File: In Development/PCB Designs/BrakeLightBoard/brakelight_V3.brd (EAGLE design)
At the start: 68.6 x 38.1 mm, 21 parts, among them Q2 30N06L

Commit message: Created brakelight board v3 board
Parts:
- moved R8 108.1 mm to (65.4, 16.6), turned to 270 degrees
- moved D2 99.1 mm to (65.4, 25.3), turned to 270 degrees
- moved R6 94.3 mm to (59.9, 32.3), turned to 270 degrees
- moved D4 93.2 mm to (58.4, 13.8)
- moved R7 84.0 mm to (39.1, 11.3), turned to 90 degrees
- moved D3 80.2 mm to (46.4, 13.9), turned to 180 degrees
- moved R4 77.8 mm to (57.6, 22.4), turned to 180 degrees
- moved R5 66.1 mm to (38.2, 19.6), turned to 90 degrees
- moved D1 61.1 mm to (32.6, 8.66)
- moved R2 49.9 mm to (36.9, 25.5), turned to 180 degrees
- moved R3 46.0 mm to (30.7, 18.4), turned to 180 degrees
- moved R1 41.8 mm to (29.7, 25.5)
- moved U$1 15.0 mm to (19.6, 23.1)
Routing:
- net GND: track 71.5 -> 0.00 mm
- net VCC: track 146.1 -> 89.0 mm
- net 5V: track 108.6 -> 62.7 mm
- net N$1: track 0.00 -> 30.3 mm
- net N$7: track 0.00 -> 15.3 mm
- net N$2: track 86.3 -> 74.4 mm
- net THRESH1: track 9.70 -> 21.1 mm
- net THRESH2: track 7.25 -> 15.8 mm
- net PT2: track 21.3 -> 29.1 mm
- net PT1: track 51.2 -> 46.1 mm
- net N$3: track 0.00 -> 3.50 mm
- net N$4: track 0.00 -> 3.21 mm
- net N$5: track 0.00 -> 2.71 mm
- net N$6: track 0.00 -> 2.39 mm

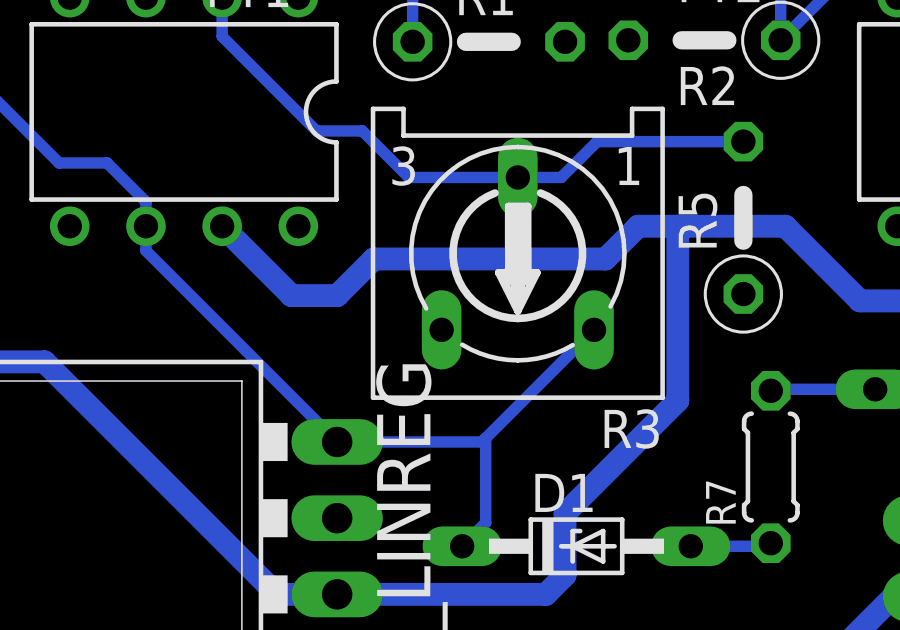
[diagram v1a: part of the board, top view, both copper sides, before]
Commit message: Improved brakelight v3 ground plane connections
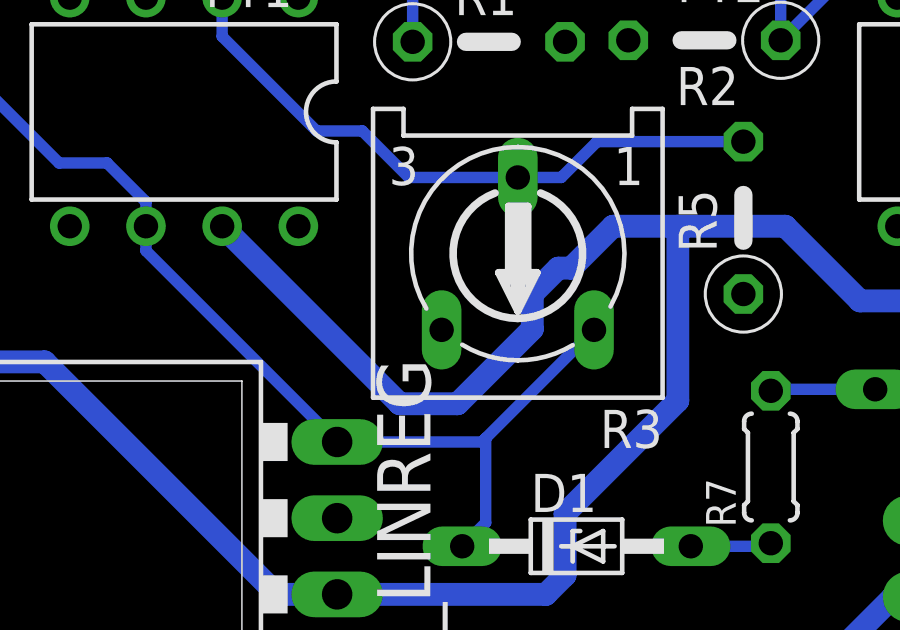
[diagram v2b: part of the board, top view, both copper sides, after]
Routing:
- net VCC: track 89.0 -> 92.7 mm
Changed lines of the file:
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@@
 <vertex x="0" y="0"/>
 </polygon>
-<wire x1="43.3324" y1="26.9494" x2="42.9332" y2="32.4626" width="0" layer="19" extent="1-1"/>
-<wire x1="15.748" y1="26.9494" x2="15.748" y2="19.3294" width="0" layer="19" extent="1-1"/>
 </signal>
 <signal name="N$2">
@@
 <wire x1="4.0894" y1="21.1858" x2="6.9464" y2="18.3288" width="0.762" layer="16"/>
 <wire x1="4.0894" y1="26.2578" x2="4.0894" y2="21.1858" width="0.762" layer="16"/>
-<wire x1="20.828" y1="19.3294" x2="23.1394" y2="17.018" width="0.762" layer="16"/>
-<wire x1="23.1394" y1="17.018" x2="24.6634" y2="17.018" width="0.762" layer="16"/>
-<wire x1="33.6042" y1="18.2372" x2="34.6964" y2="19.3294" width="0.762" layer="16"/>
-<wire x1="34.6964" y1="19.3294" x2="36.0172" y2="19.3294" width="0.762" layer="16"/>
 <wire x1="36.0172" y1="19.3294" x2="39.5986" y2="19.3294" width="0.762" layer="16"/>
 <wire x1="42.0878" y1="16.8402" x2="47.2694" y2="16.8402" width="0.762" layer="16"/>
 <wire x1="47.2694" y1="16.8402" x2="48.4124" y2="17.9832" width="0.762" layer="16"/>
 <wire x1="48.4124" y1="17.9832" x2="48.4124" y2="19.3294" width="0.762" layer="16"/>
-<wire x1="24.6634" y1="17.018" x2="25.8826" y2="18.2372" width="0.762" layer="16"/>
-<wire x1="25.8826" y1="18.2372" x2="33.6042" y2="18.2372" width="0.762" layer="16"/>
 <wire x1="39.5986" y1="19.3294" x2="42.0878" y2="16.8402" width="0.762" layer="16"/>
 <wire x1="36.0172" y1="19.3294" x2="36.0172" y2="13.5128" width="0.762" layer="16"/>
@@
 <wire x1="31.6194" y1="7.0576" x2="24.6612" y2="7.0576" width="0.762" layer="16"/>
 <wire x1="36.0172" y1="13.5128" x2="32.258" y2="9.7536" width="0.762" layer="16"/>
+<wire x1="32.4612" y1="17.9324" x2="32.0294" y2="17.9324" width="0.762" layer="16"/>
+<wire x1="32.0294" y1="17.9324" x2="31.1658" y2="17.0688" width="0.762" layer="16"/>
+<wire x1="26.7462" y1="13.4112" x2="20.828" y2="19.3294" width="0.762" layer="16"/>
+<wire x1="36.0172" y1="19.3294" x2="33.8582" y2="19.3294" width="0.762" layer="16"/>
+<wire x1="33.8582" y1="19.3294" x2="32.4612" y2="17.9324" width="0.762" layer="16"/>
+<wire x1="31.1658" y1="17.0688" x2="31.1658" y2="15.9004" width="0.762" layer="16"/>
+<wire x1="31.1658" y1="15.9004" x2="28.6766" y2="13.4112" width="0.762" layer="16"/>
+<wire x1="28.6766" y1="13.4112" x2="26.7462" y2="13.4112" width="0.762" layer="16"/>
 </signal>
 <signal name="N$1">

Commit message: Added missing resistor values
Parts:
- R7, R8: value (none) -> 1k
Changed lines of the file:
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@@
 <attribute name="VALUE" x="56.134" y="11.176" size="1.27" layer="27" ratio="10"/>
 </element>
-<element name="R7" library="0ohmresistor" package="0204/5" package3d_urn="urn:adsk.eagle:package:23488/1" value="" x="39.116" y="11.303" smashed="yes" rot="R90">
+<element name="R7" library="0ohmresistor" package="0204/5" package3d_urn="urn:adsk.eagle:package:23488/1" value="1k" x="39.116" y="11.303" smashed="yes" rot="R90">
 <attribute name="NAME" x="37.9476" y="9.2964" size="0.9906" layer="25" ratio="10" rot="R90"/>
 <attribute name="POPULARITY" value="18" x="39.116" y="11.303" size="1.778" layer="27" rot="R90" display="off"/>
@@
 <attribute name="VALUE" x="41.4274" y="9.1694" size="0.9906" layer="27" ratio="10" rot="R90"/>
 </element>
-<element name="R8" library="0ohmresistor" package="0204/5" package3d_urn="urn:adsk.eagle:package:23488/1" value="" x="65.3542" y="16.5862" smashed="yes" rot="R270">
+<element name="R8" library="0ohmresistor" package="0204/5" package3d_urn="urn:adsk.eagle:package:23488/1" value="1k" x="65.3542" y="16.5862" smashed="yes" rot="R270">
 <attribute name="NAME" x="66.5226" y="18.5928" size="0.9906" layer="25" ratio="10" rot="R270"/>
 <attribute name="POPULARITY" value="18" x="65.3542" y="16.5862" size="1.778" layer="27" rot="R270" display="off"/>

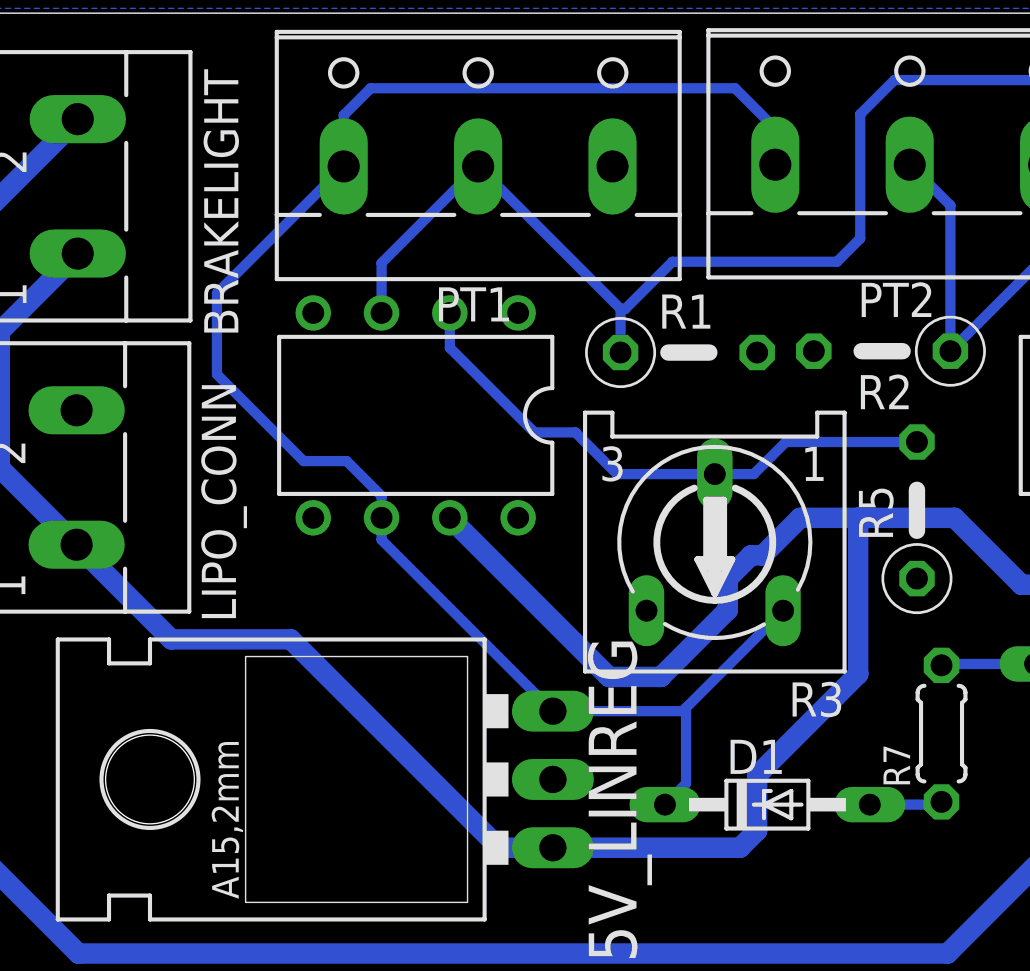
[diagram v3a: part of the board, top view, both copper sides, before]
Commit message: Created new brakelight board using TLC2252
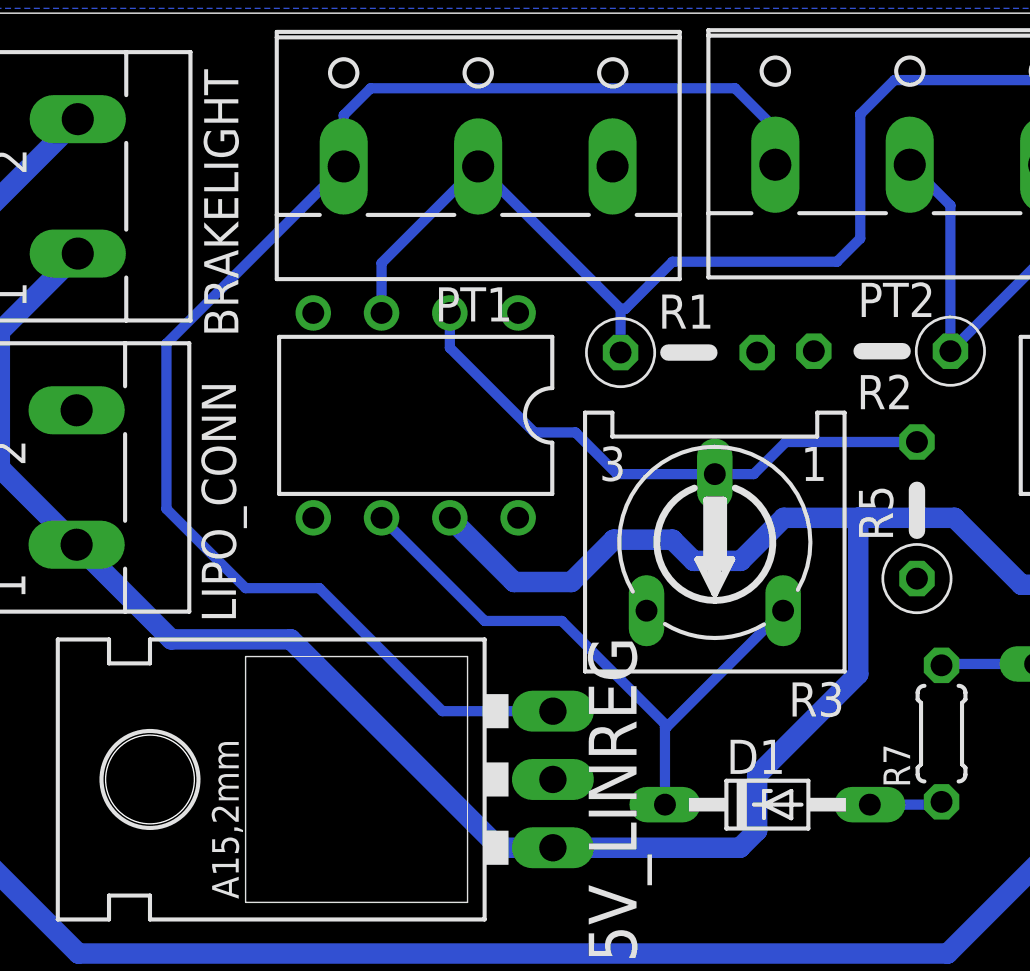
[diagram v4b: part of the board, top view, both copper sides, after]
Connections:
- new net N$8: D1.C, R3.A, U$1.6
- net 5V: no longer D1.C, R3.A, U$1.6
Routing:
- net N$8: track 0.00 -> 22.9 mm
- net 5V: track 62.7 -> 53.3 mm
- net VCC: track 92.7 -> 89.7 mm
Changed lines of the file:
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@@
 <contactref element="PT1" pad="1"/>
 <contactref element="PT2" pad="1"/>
-<contactref element="U$1" pad="6"/>
-<contactref element="R3" pad="A"/>
-<contactref element="D1" pad="C"/>
-<wire x1="33.2232" y1="15.875" x2="29.6128" y2="12.2646" width="0.381" layer="16"/>
-<wire x1="29.6128" y1="12.2646" x2="29.4858" y2="12.1376" width="0.381" layer="16"/>
-<wire x1="29.4858" y1="12.1376" x2="24.6612" y2="12.1376" width="0.381" layer="16"/>
-<wire x1="28.829" y1="8.6614" x2="29.6128" y2="9.4452" width="0.381" layer="16"/>
-<wire x1="29.6128" y1="9.4452" x2="29.6128" y2="12.2646" width="0.381" layer="16"/>
 <wire x1="17.8826" y1="35.306" x2="16.8802" y2="34.3036" width="0.381" layer="16"/>
 <wire x1="16.8802" y1="32.3986" x2="16.8802" y2="34.3036" width="0.381" layer="16"/>
@@
 <wire x1="32.9332" y1="33.8088" x2="32.9332" y2="32.4626" width="0.381" layer="16"/>
 <wire x1="17.8826" y1="35.306" x2="31.436" y2="35.306" width="0.381" layer="16"/>
-<wire x1="18.288" y1="19.3294" x2="18.288" y2="18.5108" width="0.381" layer="16"/>
-<wire x1="18.288" y1="18.5108" x2="24.6612" y2="12.1376" width="0.381" layer="16"/>
-<wire x1="16.8802" y1="32.3986" x2="12.1666" y2="27.685" width="0.381" layer="16"/>
-<wire x1="12.1666" y1="27.685" x2="12.1666" y2="24.6634" width="0.381" layer="16"/>
-<wire x1="12.1666" y1="24.6634" x2="15.3924" y2="21.4376" width="0.381" layer="16"/>
-<wire x1="15.3924" y1="21.4376" x2="16.9926" y2="21.4376" width="0.381" layer="16"/>
-<wire x1="16.9926" y1="21.4376" x2="18.288" y2="20.1422" width="0.381" layer="16"/>
-<wire x1="18.288" y1="20.1422" x2="18.288" y2="19.3294" width="0.381" layer="16"/>
+<wire x1="16.8802" y1="32.3986" x2="10.287" y2="25.8054" width="0.381" layer="16"/>
+<wire x1="10.287" y1="25.8054" x2="10.287" y2="19.6596" width="0.381" layer="16"/>
+<wire x1="20.5522" y1="12.1376" x2="24.6612" y2="12.1376" width="0.381" layer="16"/>
+<wire x1="10.287" y1="19.6596" x2="13.2334" y2="16.7132" width="0.381" layer="16"/>
+<wire x1="13.2334" y1="16.7132" x2="15.9766" y2="16.7132" width="0.381" layer="16"/>
+<wire x1="15.9766" y1="16.7132" x2="20.5522" y2="12.1376" width="0.381" layer="16"/>
 </signal>
 <signal name="PT2">
@@
 <wire x1="31.6194" y1="7.0576" x2="24.6612" y2="7.0576" width="0.762" layer="16"/>
 <wire x1="36.0172" y1="13.5128" x2="32.258" y2="9.7536" width="0.762" layer="16"/>
-<wire x1="32.4612" y1="17.9324" x2="32.0294" y2="17.9324" width="0.762" layer="16"/>
-<wire x1="32.0294" y1="17.9324" x2="31.1658" y2="17.0688" width="0.762" layer="16"/>
-<wire x1="26.7462" y1="13.4112" x2="20.828" y2="19.3294" width="0.762" layer="16"/>
-<wire x1="36.0172" y1="19.3294" x2="33.8582" y2="19.3294" width="0.762" layer="16"/>
-<wire x1="33.8582" y1="19.3294" x2="32.4612" y2="17.9324" width="0.762" layer="16"/>
-<wire x1="31.1658" y1="17.0688" x2="31.1658" y2="15.9004" width="0.762" layer="16"/>
-<wire x1="31.1658" y1="15.9004" x2="28.6766" y2="13.4112" width="0.762" layer="16"/>
-<wire x1="28.6766" y1="13.4112" x2="26.7462" y2="13.4112" width="0.762" layer="16"/>
+<wire x1="33.2486" y1="19.3294" x2="36.0172" y2="19.3294" width="0.762" layer="16"/>
+<wire x1="23.2156" y1="16.9418" x2="25.3492" y2="16.9418" width="0.762" layer="16"/>
+<wire x1="25.3492" y1="16.9418" x2="26.924" y2="18.5166" width="0.762" layer="16"/>
+<wire x1="26.924" y1="18.5166" x2="29.1084" y2="18.5166" width="0.762" layer="16"/>
+<wire x1="29.1084" y1="18.5166" x2="29.8958" y2="17.7292" width="0.762" layer="16"/>
+<wire x1="29.8958" y1="17.7292" x2="31.6484" y2="17.7292" width="0.762" layer="16"/>
+<wire x1="20.828" y1="19.3294" x2="23.2156" y2="16.9418" width="0.762" layer="16"/>
+<wire x1="31.6484" y1="17.7292" x2="33.2486" y2="19.3294" width="0.762" layer="16"/>
 </signal>
 <signal name="N$1">
@@
 <wire x1="54.5592" y1="13.8938" x2="54.61" y2="13.843" width="0.381" layer="16"/>
 </signal>
+<signal name="N$8">
+<contactref element="R3" pad="A"/>
+<contactref element="U$1" pad="6"/>
+<contactref element="D1" pad="C"/>
+<wire x1="18.288" y1="19.3294" x2="22.1234" y2="15.494" width="0.381" layer="16"/>
+<wire x1="28.829" y1="11.6586" x2="28.829" y2="11.5316" width="0.381" layer="16"/>
+<wire x1="28.829" y1="11.5316" x2="28.829" y2="8.6614" width="0.381" layer="16"/>
+<wire x1="22.1234" y1="15.494" x2="24.9936" y2="15.494" width="0.381" layer="16"/>
+<wire x1="24.9936" y1="15.494" x2="28.829" y2="11.6586" width="0.381" layer="16"/>
+<wire x1="33.2232" y1="15.875" x2="28.8798" y2="11.5316" width="0.381" layer="16"/>
+<wire x1="28.8798" y1="11.5316" x2="28.829" y2="11.5316" width="0.381" layer="16"/>
+</signal>
 </signals>
